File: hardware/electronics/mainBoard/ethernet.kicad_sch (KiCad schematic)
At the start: 34 parts, among them U4 MRJ-5381-01, U5 LAN8742AI

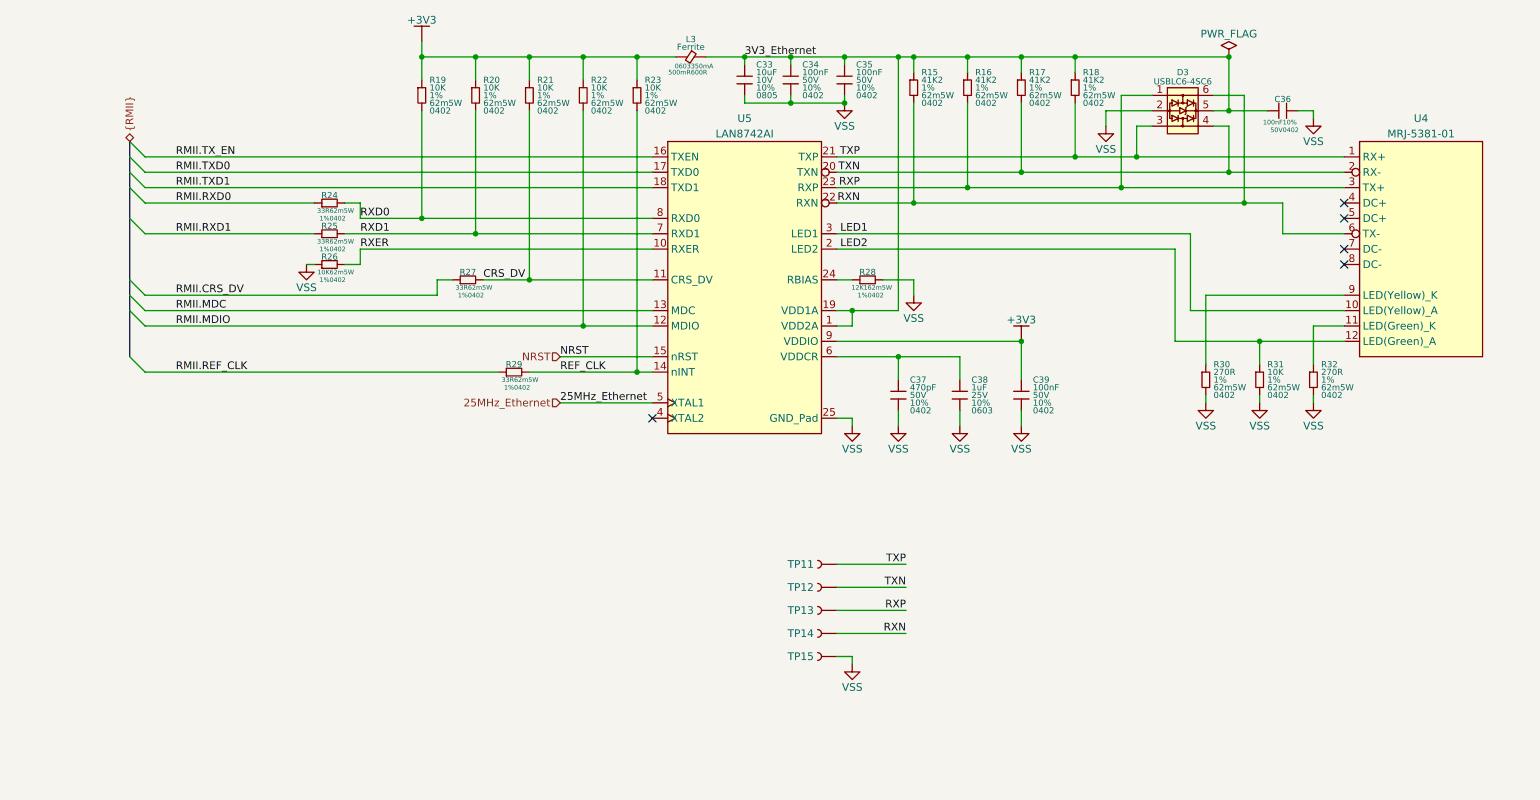
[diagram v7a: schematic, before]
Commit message: assigned footprints
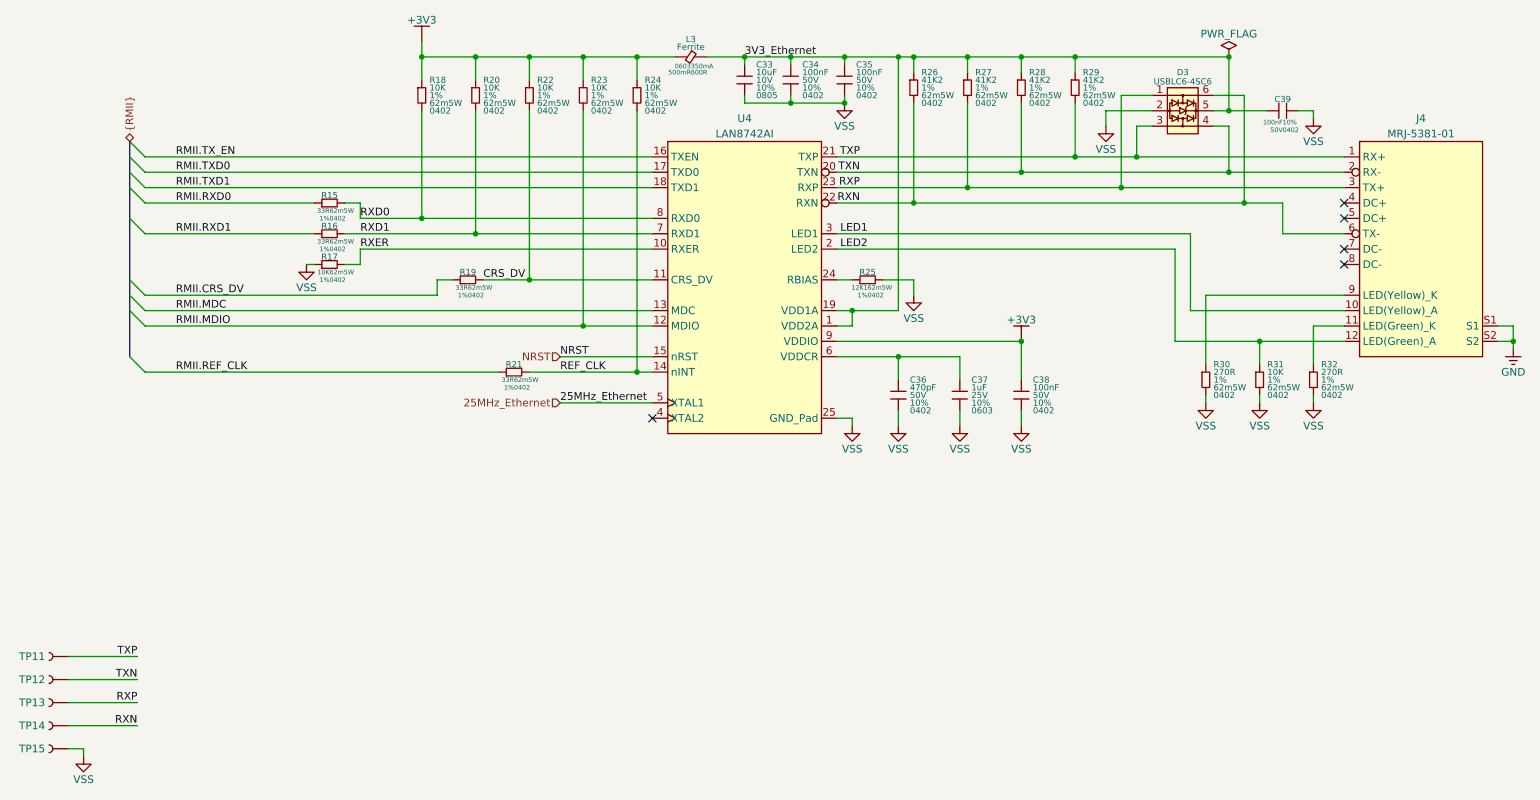
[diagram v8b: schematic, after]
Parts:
- C33: footprint (none) -> lib_passives:GCM0805
- C34, C35: footprint (none) -> lib_passives:GCM0402
- C36: renamed from C37; footprint (none) -> lib_passives:GCM0402
- C37: renamed from C38; footprint (none) -> lib_passives:GRT0603
- C38: renamed from C39; footprint (none) -> lib_passives:GCM0402
- C39: renamed from C36; footprint (none) -> lib_passives:GCM0402
- L3: footprint (none) -> lib_passives:L_0603
- R15: renamed from R24; footprint (none) -> lib_passives:CRCW0402
- R16: renamed from R25; footprint (none) -> lib_passives:CRCW0402
- R17: renamed from R26; footprint (none) -> lib_passives:CRCW0402
- R18: renamed from R19; footprint (none) -> lib_passives:CRCW0402
- R19: renamed from R27; footprint (none) -> lib_passives:CRCW0402
- R20, R30, R31, R32: footprint (none) -> lib_passives:CRCW0402
- R21: renamed from R29; footprint (none) -> lib_passives:CRCW0402
- R22: renamed from R21; footprint (none) -> lib_passives:CRCW0402
- R23: renamed from R22; footprint (none) -> lib_passives:CRCW0402
- R24: renamed from R23; footprint (none) -> lib_passives:CRCW0402
- R25: renamed from R28; footprint (none) -> lib_passives:CRCW0402
- R26: renamed from R15; footprint (none) -> lib_passives:CRCW0402
- R27: renamed from R16; footprint (none) -> lib_passives:CRCW0402
- R28: renamed from R17; footprint (none) -> lib_passives:CRCW0402
- R29: renamed from R18; footprint (none) -> lib_passives:CRCW0402
- TP11, TP12, TP13, TP14: footprint (none) -> lib_misc:TP_2mm
- TP15: footprint (none) -> lib_misc:TP_RCW
- renumbered U4 to J4, U5 to U4
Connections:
- new net GND: J4.S1, J4.S2
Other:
- moved on the sheet: TP11, TP12, TP13, TP14, TP15
